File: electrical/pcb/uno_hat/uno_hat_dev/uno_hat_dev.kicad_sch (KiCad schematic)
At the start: 96 parts, among them Q1 NMOS, Q10 NMOS, Q11 NMOS, Q12 NMOS, Q13 NMOS, Q14 PMOS, Q15 PMOS, Q16 PMOS, Q17 PMOS, Q2 PMOS, Q20 NMOS, Q3 NPN, Q4 NMOS, Q5 PMOS, Q6 NMOS, Q7 PMOS, Q8 NMOS, Q9 PMOS, T2 Transformer_1P_1S, U5 LM5185QPWPRQ1, U6 INA219AxD

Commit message: schematic done
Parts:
- Q20: footprint (none) -> Package_TO_SOT_THT:TO-220-3_Vertical
- U5: footprint PWP0014G-IPC_A -> Package_SO:Texas_HTSSOP-14-1EP_4.4x5mm_P0.65mm_EP3.4x5mm_Mask3.155x3.255mm
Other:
- note added: "CSD19534KCS"
- note added: "Leakage L: 4.04e-6 Lp (uH):202.00 NS1-NP: 4.00"
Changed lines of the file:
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@@
 		)
 	)
+	(text "Leakage L: 4.04e-6\nLp (uH):202.00\nNS1-NP: 4.00\n"
+		(exclude_from_sim no)
+		(at 225.044 140.208 0)
+		(effects
+			(font
+				(size 1.27 1.27)
+			)
+		)
+	)
+	(text "CSD19534KCS"
+		(exclude_from_sim no)
+		(at 206.502 135.636 0)
+		(effects
+			(font
+				(size 1.27 1.27)
+			)
+		)
+	)
 	(junction
 		(at 186.69 154.94)
@@
 			)
 		)
-		(property "Footprint" ""
+		(property "Footprint" "Package_TO_SOT_THT:TO-220-3_Vertical"
 			(at 201.93 129.54 0)
 			(effects
@@
 			)
 		)
-		(property "Footprint" "PWP0014G-IPC_A"
+		(property "Footprint" "Package_SO:Texas_HTSSOP-14-1EP_4.4x5mm_P0.65mm_EP3.4x5mm_Mask3.155x3.255mm"
 			(at 140.97 127 0)
 			(effects

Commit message: started layout
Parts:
- added J1, J2: Conn_01x08_MountingPin, Connector_FFC-FPC:Amphenol_F32Q-1A7x1-11008_1x08-1MP_P0.5mm_Horizontal, symbol Connector_Generic_MountingPin:Conn_01x08_MountingPin
- R45, R47: footprint Resistor_THT:R_Axial_DIN0207_L6.3mm_D2.5mm_P7.62mm_Horizontal -> Resistor_SMD:R_0805_2012Metric
- R46: footprint Resistor_SMD:R_0402_1005Metric -> Resistor_SMD:R_0805_2012Metric
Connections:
- net +12V: no longer C13.2, C18.2, C19.2, Css2.2, Cvcc2.2, R42.1, Rcs2.1, U5.15 (EP), U5.5 (AGND), U5.8 (PGND)
- net DOT1: now also J1.1 (Pin_1)
- net DOT2: now also J1.2 (Pin_2)
- net DOT3: now also J1.3 (Pin_3)
- net DOT4: now also J1.4 (Pin_4)
- net DOT5: now also J1.5 (Pin_5)
- net DOT6: now also J1.6 (Pin_6)
- net DOT7: now also J1.7 (Pin_7)
- net DOT8: now also J1.8 (Pin_8)
- net DOWN7: now also A1.11 (A2); no longer A1.9 (A0)
- net PWR_EN: now also A1.9 (A0); no longer A1.11 (A2)
- new net GNDA: C13.2, C18.2, C19.2, Css2.2, Cvcc2.2, J2.1 (Pin_1), J2.2 (Pin_2), J2.3 (Pin_3), J2.4 (Pin_4), J2.5 (Pin_5), J2.6 (Pin_6), J2.7 (Pin_7), J2.8 (Pin_8), R42.1, Rcs2.1, U5.15 (EP), U5.5 (AGND), U5.8 (PGND)
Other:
- moved on the sheet: C18, C19, R45

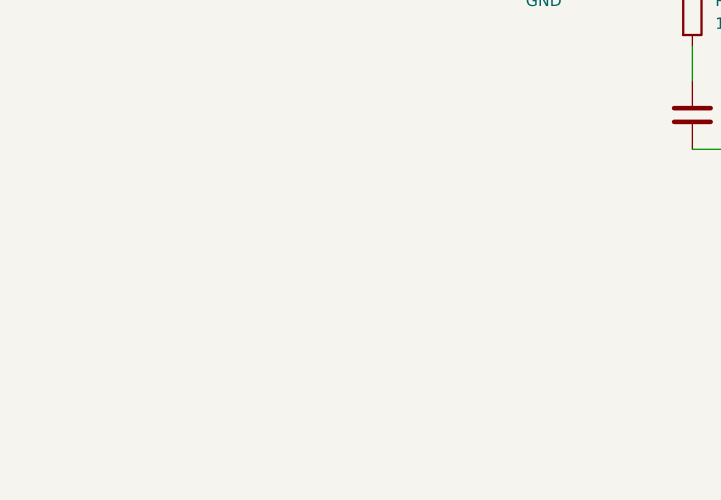
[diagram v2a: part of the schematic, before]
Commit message: ECE day demo board added
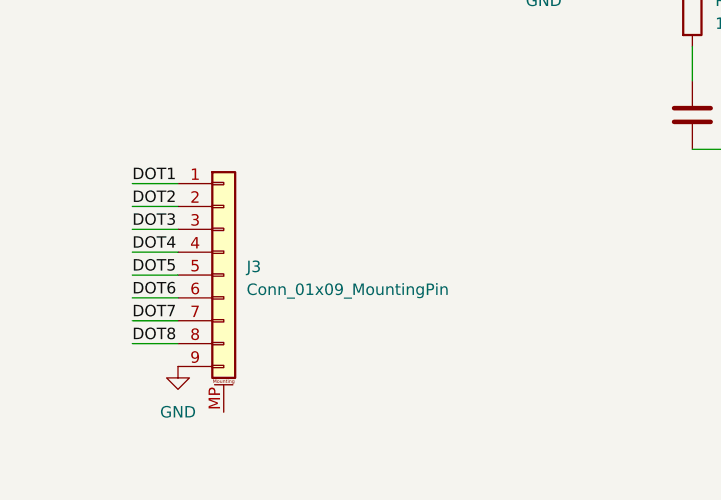
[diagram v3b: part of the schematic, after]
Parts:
- added J3: Conn_01x09_MountingPin, symbol Connector_Generic_MountingPin:Conn_01x09_MountingPin
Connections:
- net DOT1: now also J3.1 (Pin_1)
- net DOT2: now also J3.2 (Pin_2)
- net DOT3: now also J3.3 (Pin_3)
- net DOT4: now also J3.4 (Pin_4)
- net DOT5: now also J3.5 (Pin_5)
- net DOT6: now also J3.6 (Pin_6)
- net DOT7: now also J3.7 (Pin_7)
- net DOT8: now also J3.8 (Pin_8)
- net GND: now also J3.9 (Pin_9)
